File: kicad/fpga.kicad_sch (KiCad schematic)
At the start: 110 parts, among them Q4 BSS138LT1G, U1 XC7A100T-2FGG676I, X4 50MHz CMOS

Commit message: Tools: honest gate verdicts, source-side island ownership, key posts at their rows, J1 pads clear of the holes, budget checks for capacitance, inductors and sources
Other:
- note added: "X4 system clock"
- note removed: "system clock"
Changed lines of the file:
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@@
 	(text "The XC7A100T has two quads of multi-gigabit transceivers (GTP). Rev A uses none of them, but UG482 Tables 5-5\nand 5-6 still want their supplies powered, their receive inputs grounded and one 100 ohm 1 % calibration\nresistor per quad to MGTAVTT. These two resistors are that." (at 412.75 1131.57 0) (effects (font (size 1.5 1.5) (italic yes)) (justify left top)))
 	(rectangle (start 590.55 1122.68) (end 758.19 1188.72) (stroke (width 0.15) (type dash)) (fill (type none)))
-	(text "system clock" (at 593.09 1126.49 0) (effects (font (size 2.2 2.2) (thickness 0.3)) (justify left)))
+	(text "X4 system clock" (at 593.09 1126.49 0) (effects (font (size 2.2 2.2) (thickness 0.3)) (justify left)))
 	(text "The FPGA's own clock. X4 runs at 50 MHz from power-on and enters bank 14 on a clock-capable (MRCC) ball, so it\ncan feed an MMCM and make any frequency the design needs. Without it nothing in the fabric would run until a\nnetwork link came up." (at 593.09 1131.57 0) (effects (font (size 1.5 1.5) (italic yes)) (justify left top)))
 	(symbol (lib_id "odin:XC7A100T-2FGG676I") (at 114.3 92.71 0) (unit 1)

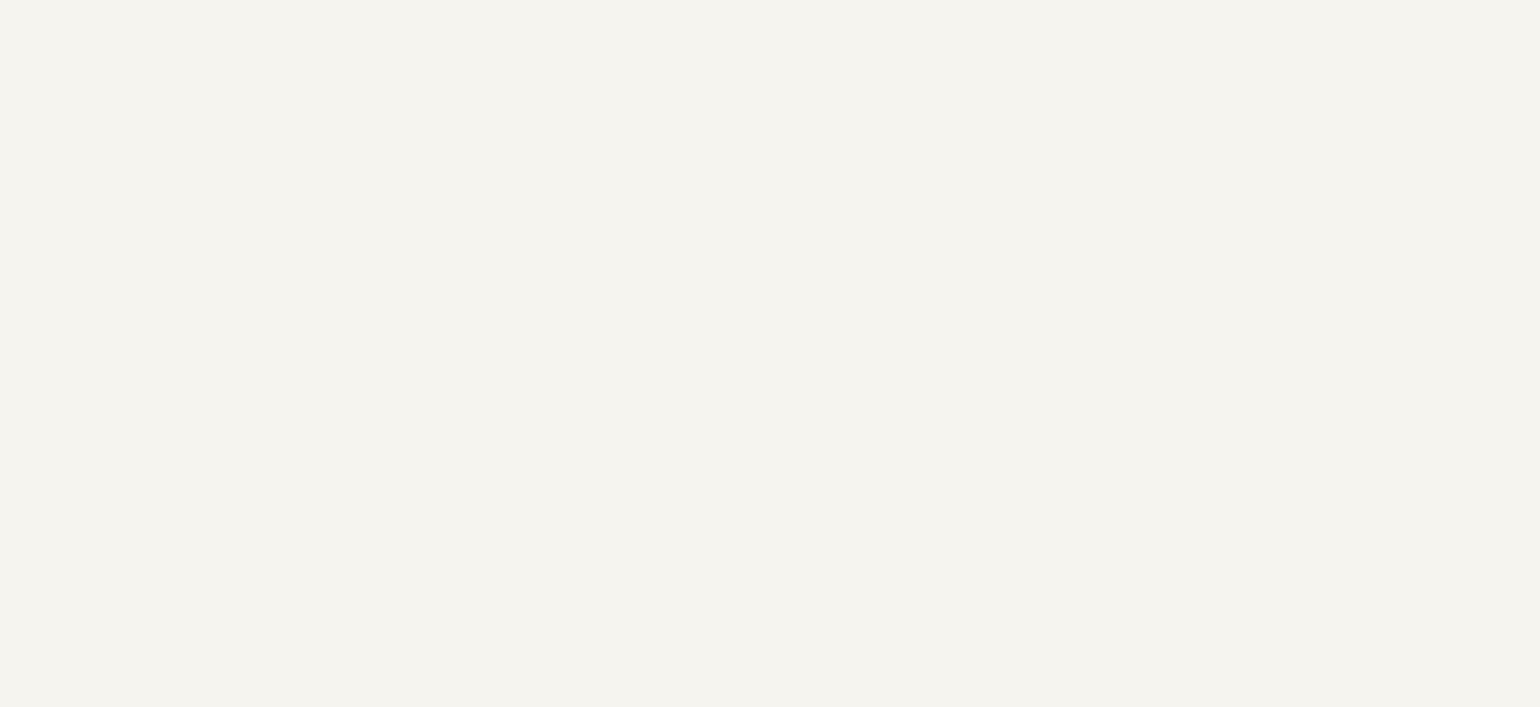
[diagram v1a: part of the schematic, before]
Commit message: Re-audit corrections, part 1: U34 selects by intent (Q6 hold, Q7 screw input), FCS_B pull-up, TPS22953 PG grounded, IN2 bypass, budget per path with recovery accounting, source policy
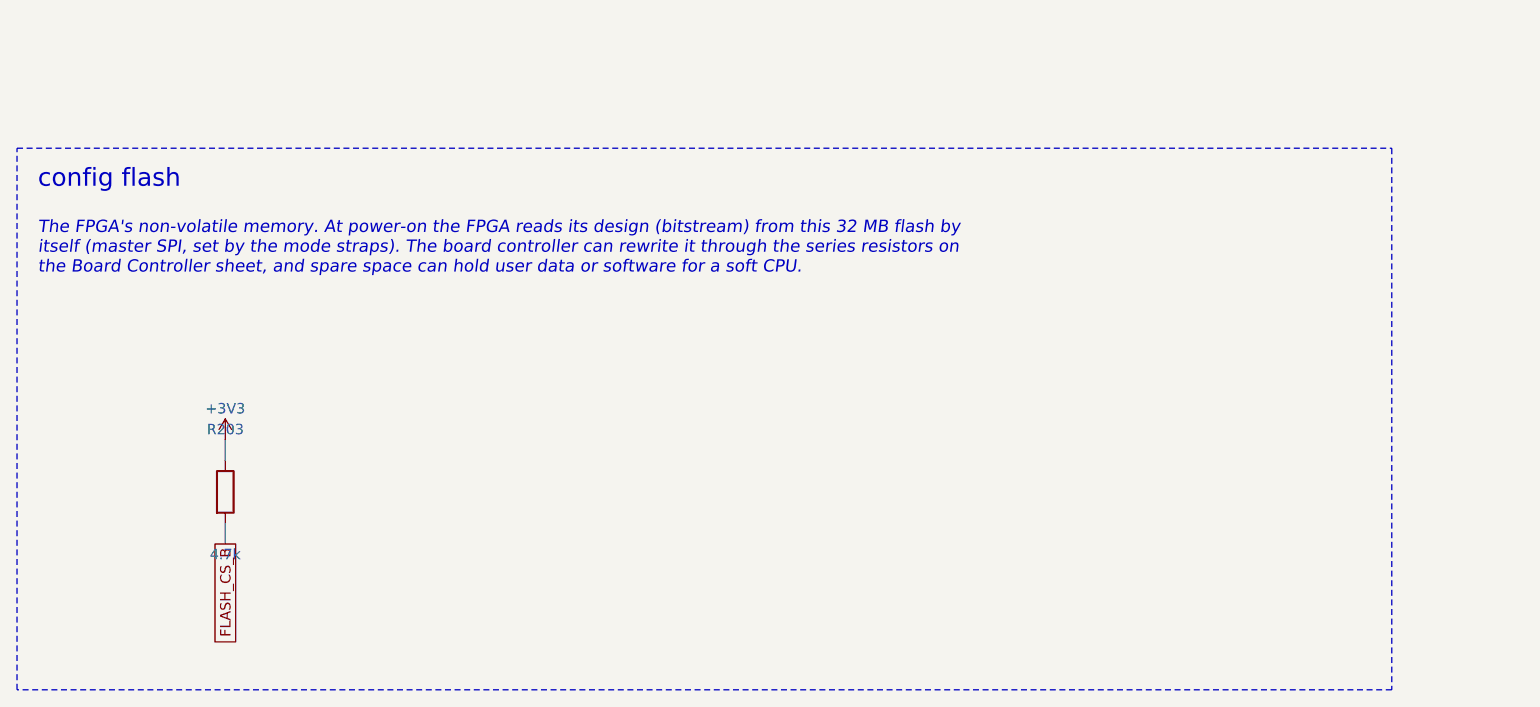
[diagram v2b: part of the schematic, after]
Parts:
- added R203: 4.7k, Resistor_SMD:R_0402_1005Metric, symbol Device:R
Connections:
- net +3V3: now also R203.1
- net FLASH_CS_B: now also R203.2
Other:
- note added: "The FPGA's non-volatile memory. At power-on the FPGA reads its design (bitstream) from this 32 MB flash by itself (master SPI, set by the mode straps). The board controller can rewrite it through the series resistors on the Board Controller sheet, and spare space can hold user data or software for a soft CPU."
- note added: "config flash"
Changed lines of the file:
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@@
 	(generator "odin-tools")
 	(generator_version "9.0")
-	(paper "User" 820 1261)
+	(paper "User" 820 1347)
 	(text "FPGA  —  FPGA, decoupling and configuration straps  —  HW 0.1.0-proto.1" (at 40 20 0) (effects (font (size 4 4) (thickness 0.6)) (justify left)))
 	(rectangle (start 30.48 41.91) (end 646.43 521.97) (stroke (width 0.15) (type dash)) (fill (type none)))
@@
 	(text "X4 system clock" (at 593.09 1126.49 0) (effects (font (size 2.2 2.2) (thickness 0.3)) (justify left)))
 	(text "The FPGA's own clock. X4 runs at 50 MHz from power-on and enters bank 14 on a clock-capable (MRCC) ball, so it\ncan feed an MMCM and make any frequency the design needs. Without it nothing in the fabric would run until a\nnetwork link came up." (at 593.09 1131.57 0) (effects (font (size 1.5 1.5) (italic yes)) (justify left top)))
+	(rectangle (start 30.48 1210.31) (end 198.12 1276.35) (stroke (width 0.15) (type dash)) (fill (type none)))
+	(text "config flash" (at 33.02 1214.12 0) (effects (font (size 2.2 2.2) (thickness 0.3)) (justify left)))
+	(text "The FPGA's non-volatile memory. At power-on the FPGA reads its design (bitstream) from this 32 MB flash by\nitself (master SPI, set by the mode straps). The board controller can rewrite it through the series resistors on\nthe Board Controller sheet, and spare space can hold user data or software for a soft CPU." (at 33.02 1219.2 0) (effects (font (size 1.5 1.5) (italic yes)) (justify left top)))
 	(symbol (lib_id "odin:XC7A100T-2FGG676I") (at 114.3 92.71 0) (unit 1)
 		(exclude_from_sim no) (in_bom yes) (on_board yes) (dnp no)
@@
 		(instances (project "odin" (path "/c44fb7fe-6133-ad34-68fd-fb66126197ef/8cec9eb4-56b4-e78b-2213-febb3af15411" (reference "#PWR0441") (unit 1))))
 	)
+	(symbol (lib_id "Device:R") (at 55.88 1252.22 0) (unit 1)
+		(exclude_from_sim no) (in_bom yes) (on_board yes) (dnp no)
+		(property "Reference" "R203" (at 55.88 1244.6 0) (effects (font (size 1.27 1.27))))
+		(property "Value" "4.7k" (at 55.88 1259.84 0) (effects (font (size 1.27 1.27))))
+		(property "Footprint" "Resistor_SMD:R_0402_1005Metric" (at 55.88 1259.84 0) (effects (font (size 1.27 1.27)) (hide yes)))
+		(property "LCSC" "C25900" (at 55.88 1259.84 0) (effects (font (size 1.27 1.27)) (hide yes)))
+		(property "Description" "4.7k pull-up of FLASH_CS_B to +3V3, for U6 (FPGA configuration flash)" (at 55.88 1259.84 0) (effects (font (size 1.27 1.27)) (hide yes)))
+		(instances (project "odin" (path "/c44fb7fe-6133-ad34-68fd-fb66126197ef/8cec9eb4-56b4-e78b-2213-febb3af15411" (reference "R203") (unit 1))))
+	)
+	(wire (pts (xy 55.88 1248.41) (xy 55.88 1245.87)) (stroke (width 0) (type default)))
+	(symbol (lib_id "power:+3V3") (at 55.88 1245.87 0) (unit 1)
+		(exclude_from_sim no) (in_bom no) (on_board yes) (dnp no)
+		(property "Reference" "#PWR0442" (at 55.88 1245.87 0) (effects (font (size 1.27 1.27)) (hide yes)))
+		(property "Value" "+3V3" (at 55.88 1242.06 0) (effects (font (size 1.27 1.27))))
+		(instances (project "odin" (path "/c44fb7fe-6133-ad34-68fd-fb66126197ef/8cec9eb4-56b4-e78b-2213-febb3af15411" (reference "#PWR0442") (unit 1))))
+	)
+	(wire (pts (xy 55.88 1256.03) (xy 55.88 1258.57)) (stroke (width 0) (type default)))
+	(global_label "FLASH_CS_B" (shape passive) (at 55.88 1258.57 90) (fields_autoplaced yes) (effects (font (size 1.27 1.27)) (justify right)))
 )
